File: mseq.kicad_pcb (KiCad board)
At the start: 2 copper layers, 100 x 65 mm, 66 parts, among them J1 Screen_I2C, J2 TC2030-NL, P1 USB_C_Plug_USB2.0, SW1 RESET, SW2 ON/OFF, SW3 MS/SLAVE, SW4 BOOT, U1 SN74AHCT125DR, U2 H11L1M, U3 MCP1703Ax-330xxTT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

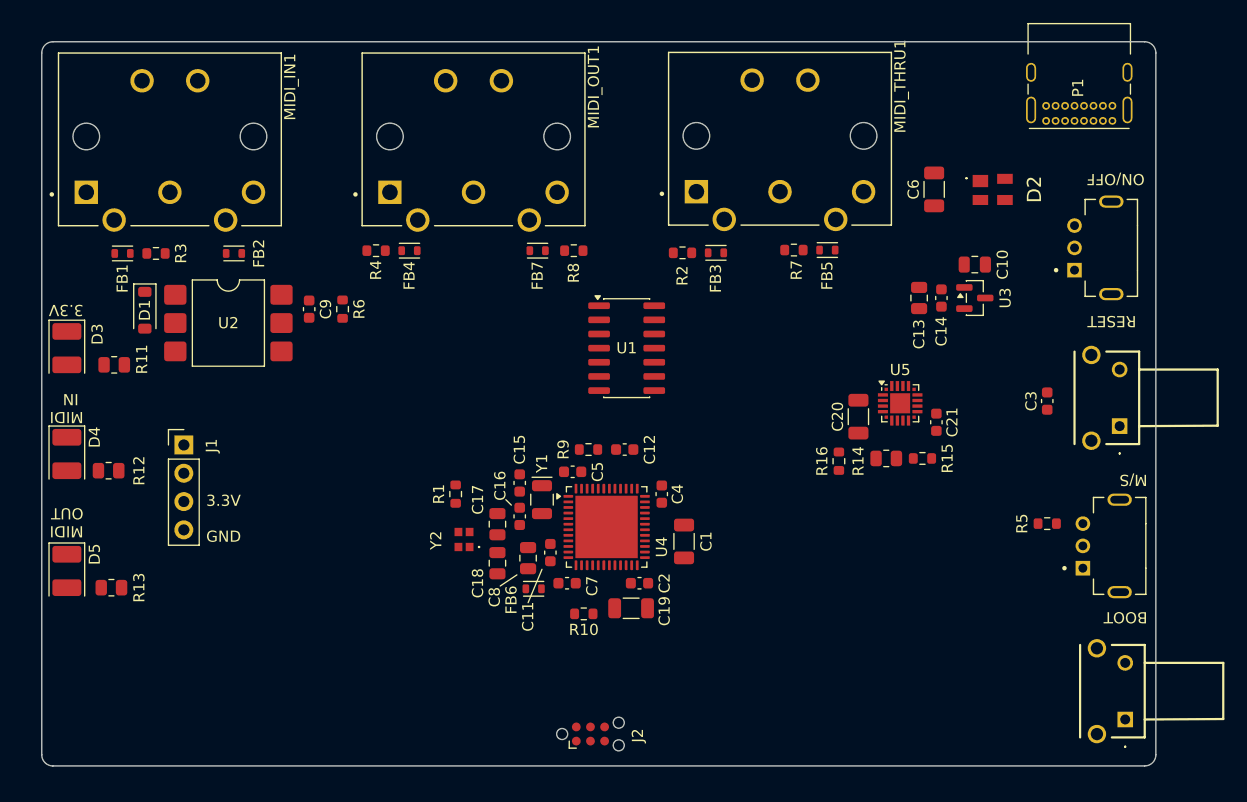
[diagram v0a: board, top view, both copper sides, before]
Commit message: 90% Routing
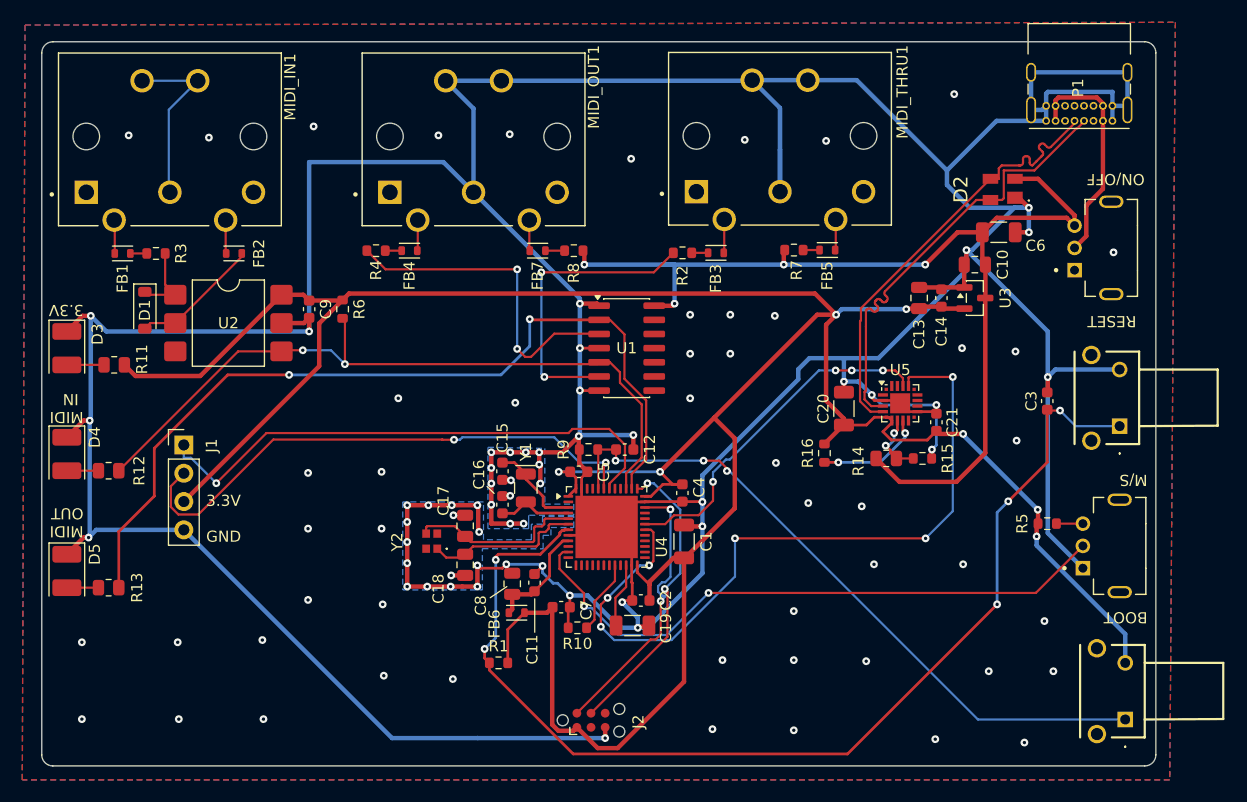
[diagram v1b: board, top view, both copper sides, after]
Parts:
- moved R1 15.6 mm to (91.0, 105.8), turned to 180 degrees
- moved C6 6.96 mm to (135.9, 67.1), turned to 0 degrees
- moved C11 3.05 mm to (94.2, 98.5)
- moved C17 2.90 mm to (88.0, 93.5)
- moved C18 2.90 mm to (88.0, 97.0)
- moved Y2 2.90 mm to (85.0, 94.8)
- moved C8 2.71 mm to (92.2, 98.7)
- moved FB6 2.64 mm to (92.6, 101.2)
- moved C7 2.21 mm to (96.6, 100.8)
- moved C15 1.87 mm to (91.3, 88.5)
- moved C16 1.87 mm to (91.3, 91.5)
- moved C4 1.85 mm to (107.5, 90.5)
- moved Y1 1.79 mm to (93.5, 90.0)
- moved C19 1.56 mm to (103.0, 102.4)
- moved C2 1.56 mm to (103.8, 100.2)
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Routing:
- net GND: track 0.00 -> 543.8 mm, vias 0 -> 104
- net +3.3V: track 0.00 -> 268.8 mm, vias 0 -> 7
- net /NRST: track 0.00 -> 99.4 mm, vias 0 -> 5
- net VBUS: track 0.00 -> 94.5 mm, vias 0 -> 4
- net /A15: track 0.00 -> 78.0 mm, vias 0 -> 2
- net /A9: track 0.00 -> 67.4 mm, vias 0 -> 6
- net /B3: track 0.00 -> 66.5 mm, vias 0 -> 2
- net /BOOT0: track 0.00 -> 61.7 mm, vias 0 -> 3
- net /A1: track 0.00 -> 55.6 mm, vias 0 -> 2
- net /B7: track 0.00 -> 49.1 mm, vias 0 -> 2
- net /B6: track 0.00 -> 48.8 mm, vias 0 -> 1
- net /D-: track 0.00 -> 40.0 mm
- net /D+: track 0.00 -> 40.0 mm
- net /A10: track 0.00 -> 31.4 mm, vias 0 -> 4
- net Net-(R4-Pad2): track 0.00 -> 29.9 mm, vias 0 -> 2
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- added copper zone on B.Cu, net GND
- added copper zone on F.Cu, net GND

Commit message: finish routing
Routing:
- net GND: vias 104 -> 108

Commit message: Last DRC Check
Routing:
- net GND: vias 108 -> 114
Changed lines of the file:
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@@
 	)
 	(segment
+		(start 91.4 97.2)
+		(end 91.7 96.9)
+		(width 0.4)
+		(layer "F.Cu")
+		(net 1)
+	)
+	(segment
 		(start 104.162 91.275)
 		(end 104.138 91.3)
@@
 	)
 	(segment
-		(start 89.35 97.25)
-		(end 89.1 97)
-		(width 0.25)
-		(layer "F.Cu")
-		(net 1)
-	)
-	(segment
 		(start 102.95 96.9875)
 		(end 102.95 98.525)
@@
 	)
 	(segment
-		(start 91.7 96.9)
-		(end 91.35 97.25)
-		(width 0.25)
-		(layer "F.Cu")
-		(net 1)
-	)
-	(segment
 		(start 91.35 90.775)
 		(end 92.025 90.775)
@@
 	)
 	(segment
-		(start 91.35 97.25)
-		(end 89.35 97.25)
-		(width 0.25)
+		(start 89.3 97.2)
+		(end 91.4 97.2)
+		(width 0.4)
 		(layer "F.Cu")
 		(net 1)
@@
 	)
 	(segment
+		(start 89.1 97)
+		(end 89.3 97.2)
+		(width 0.4)
+		(layer "F.Cu")
+		(net 1)
+	)
+	(segment
 		(start 84.6 98.9)
 		(end 86.7 98.9)
@@
 	)
 	(via
+		(at 69.1 81.5)
+		(size 0.7)
+		(drill 0.3)
+		(layers "F.Cu" "B.Cu")
+		(free yes)
+		(net 1)
+	)
+	(via
 		(at 111.8 74.5)
 		(size 0.7)
@@
 	)
 	(via
+		(at 66.5 84.2)
+		(size 0.7)
+		(drill 0.3)
+		(layers "F.Cu" "B.Cu")
+		(free yes)
+		(net 1)
+	)
+	(via
 		(at 82.8 96.8)
 		(size 0.7)
@@
 	)
 	(via
+		(at 82.1 75.9)
+		(size 0.7)
+		(drill 0.3)
+		(layers "F.Cu" "B.Cu")
+		(free yes)
+		(net 1)
+	)
+	(via
 		(at 140.3 80.1)
 		(size 0.7)
@@
 	)
 	(via
+		(at 88.3 75.9)
+		(size 0.7)
+		(drill 0.3)
+		(layers "F.Cu" "B.Cu")
+		(free yes)
+		(net 1)
+	)
+	(via
 		(at 92.05 90.75)
 		(size 0.7)
@@
 	)
 	(via
+		(at 93.9 107.4)
+		(size 0.7)
+		(drill 0.3)
+		(layers "F.Cu" "B.Cu")
+		(free yes)
+		(net 1)
+	)
+	(via
 		(at 84.6 98.9)
 		(size 0.7)
@@
 	)
 	(via
+		(at 142.8 61)
+		(size 0.7)
+		(drill 0.3)
+		(layers "F.Cu" "B.Cu")
+		(free yes)
+		(net 1)
+	)
+	(via
 		(at 108.2 74.5)
 		(size 0.7)
@@
 		(filled_areas_thickness no)
 		(keepout
-			(tracks not_allowed)
+			(tracks allowed)
 			(vias not_allowed)
 			(pads not_allowed)
@@
 		(polygon
 			(pts
-				(xy 89.6 99.4) (xy 89.6 97.6) (xy 89.8 97.6) (xy 89.8 99.6) (xy 82.1 99.6) (xy 82.1 99.4)
+				(xy 89.6 99.4) (xy 89.6 97.1) (xy 89.8 97.1) (xy 89.8 99.6) (xy 82.1 99.6) (xy 82.1 99.4)
 			)
 		)
@@
 		(filled_areas_thickness no)
 		(keepout
-			(tracks not_allowed)
+			(tracks allowed)
 			(vias not_allowed)
 			(pads allowed)
@@
 		(polygon
 			(pts
-				(xy 98 91.6) (xy 95.35 91.6) (xy 95.2 91.5) (xy 95.2 87.1) (xy 95.45 87.1) (xy 95.45 91.35) (xy 95.6 91.45)
+				(xy 98 91.6) (xy 95.35 91.6) (xy 95.2 91.5) (xy 95.2 86.8) (xy 95.45 86.8) (xy 95.45 91.35) (xy 95.6 91.45)
 				(xy 98 91.45)
 			)
@@
 		(filled_areas_thickness no)
 		(keepout
-			(tracks not_allowed)
+			(tracks allowed)
 			(vias not_allowed)
 			(pads not_allowed)
@@
 		(polygon
 			(pts
-				(xy 89.6 97) (xy 89.6 95.5) (xy 94.5 95.5) (xy 94.8 95.1) (xy 94.8 94.2) (xy 95.2 94.2) (xy 95.7 93.7)
+				(xy 89.6 97.2) (xy 89.6 95.5) (xy 94.5 95.5) (xy 94.8 95.1) (xy 94.8 94.2) (xy 95.2 94.2) (xy 95.7 93.7)
 				(xy 95.7 93.55) (xy 96.6 93.55) (xy 96.6 93.7) (xy 96 93.7) (xy 95.2 94.4) (xy 95 94.4) (xy 95 95.1)
-				(xy 94.6 95.7) (xy 89.8 95.7) (xy 89.8 97)
+				(xy 94.6 95.7) (xy 89.8 95.7) (xy 89.8 97.2)
 			)
 		)
@@
 		(filled_areas_thickness no)
 		(keepout
-			(tracks not_allowed)
+			(tracks allowed)
 			(vias not_allowed)
 			(pads not_allowed)
@@
 		(polygon
 			(pts
-				(xy 95.45 86.5) (xy 95.2 86.5) (xy 95.2 86.4) (xy 89.95 86.4) (xy 89.95 93.8) (xy 93.65 93.8) (xy 93.65 93.9)
+				(xy 95.45 86.9) (xy 95.2 86.9) (xy 95.2 86.4) (xy 89.95 86.4) (xy 89.95 93.8) (xy 93.65 93.8) (xy 93.65 93.9)
 				(xy 89.85 93.9) (xy 89.85 86.3) (xy 95.45 86.3)
 			)

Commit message: v0.1.0 done
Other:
- board text added: "MSeq v0.1.0"

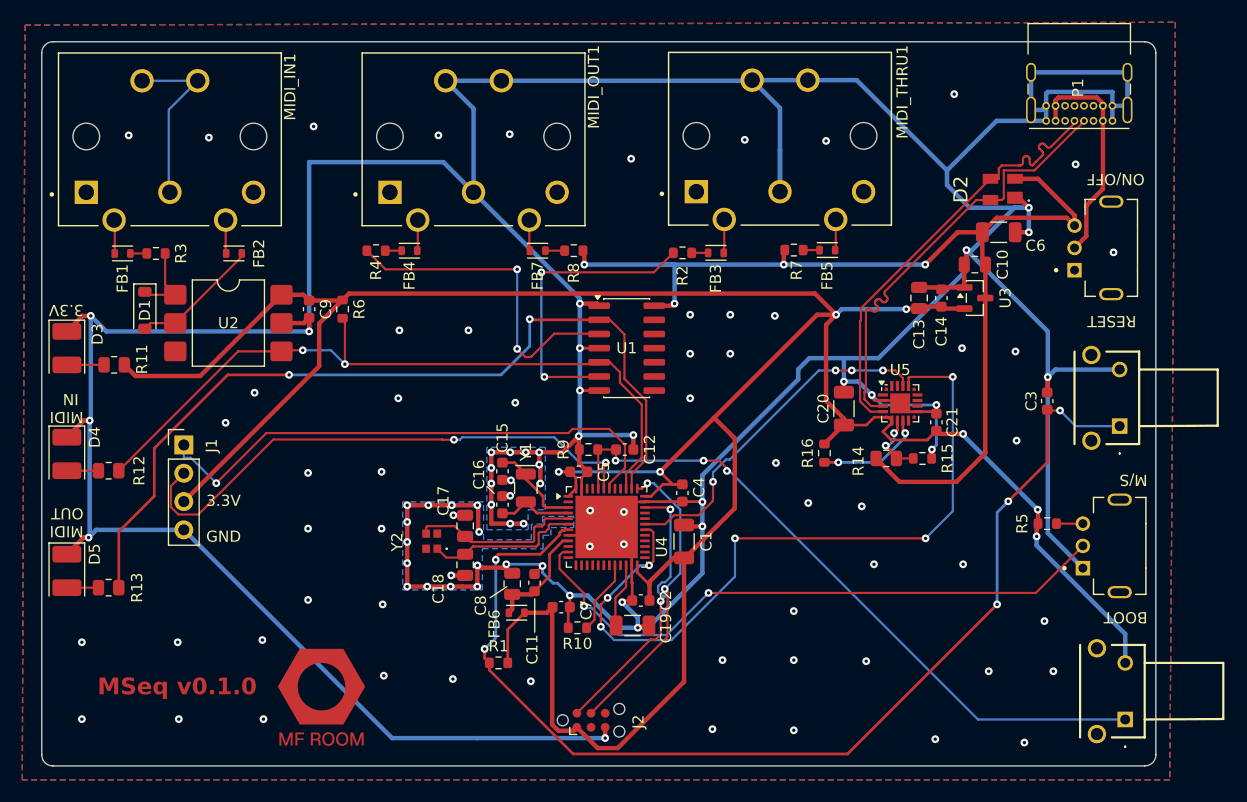
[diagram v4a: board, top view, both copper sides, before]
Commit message: LCSC Part Change, need MCP/MPN
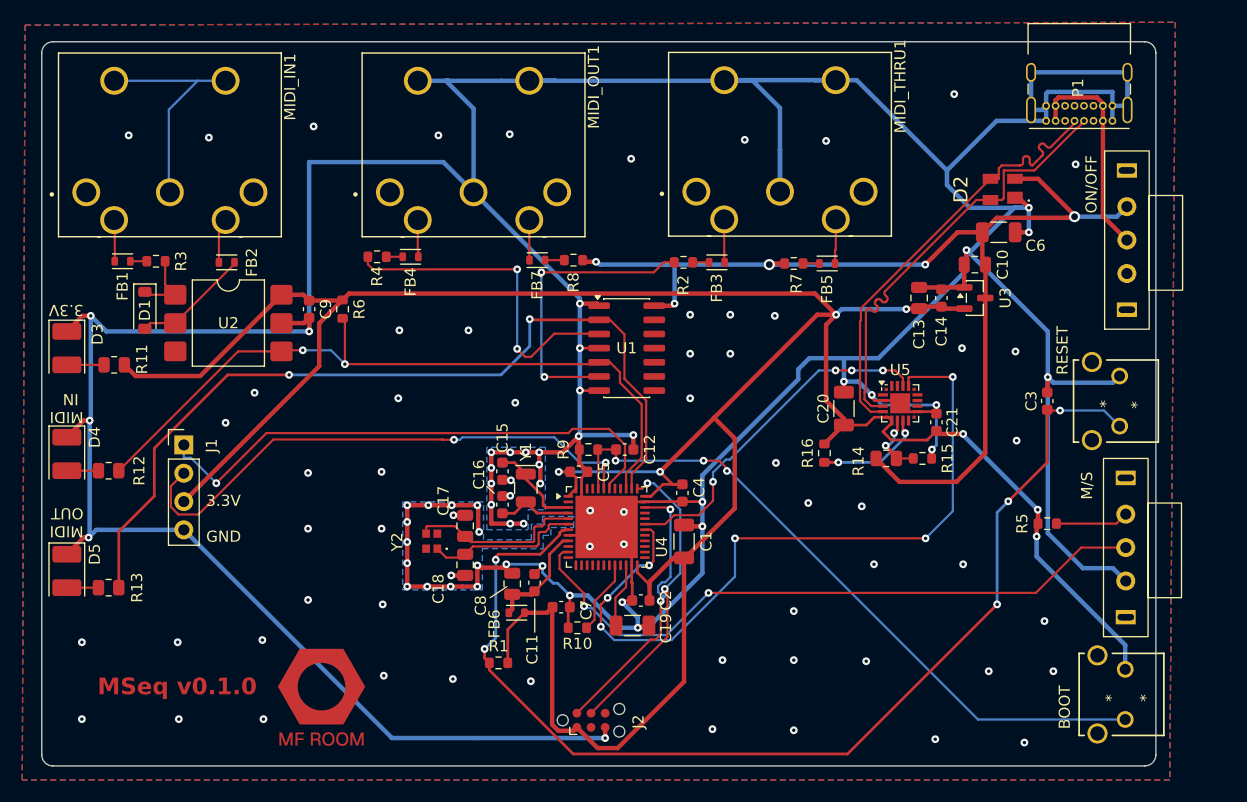
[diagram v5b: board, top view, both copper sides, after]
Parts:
- MIDI_IN1, MIDI_OUT1, MIDI_THRU1: footprint mseq_lib:SWITCHCRAFT_57PC5F -> mseq_lib:DIN-504
- SW1, SW4: footprint mseq_lib:TL6110DF160QP -> mseq_lib:SW2_1825027-A_TEC
- SW2, SW3: footprint mseq_lib:SW_SLW-874744-6A-RA-N-D -> mseq_lib:SK-12E12-G5
- moved SW3 3.20 mm to (147.3, 98.4)
- moved SW2 2.69 mm to (147.4, 70.8)
- moved FB5 1.21 mm to (120.5, 69.9)
- moved R7 1.21 mm to (117.5, 69.9)
- moved FB2 1.03 mm to (66.6, 69.8)
- moved FB3 0.86 mm to (110.6, 69.8)
- moved R2 0.86 mm to (107.6, 69.8)
- moved FB7 0.85 mm to (94.5, 69.6)
- moved R8 0.85 mm to (97.7, 69.6)
- moved FB1 0.70 mm to (57.2, 69.7)
- moved R3 0.70 mm to (60.2, 69.7)
- moved FB4 0.56 mm to (83.1, 69.3)
- moved R4 0.56 mm to (80.1, 69.3)
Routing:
- net GND: track 543.8 -> 557.7 mm, vias 114 -> 113
- net unconnected-(MIDI_IN1-GND-PadG1): track 16.1 -> 21.1 mm
- net Net-(SW3-A): track 2.38 -> 6.58 mm
- net /A1: track 55.6 -> 59.3 mm
- net VBUS: track 94.5 -> 97.9 mm, vias 4 -> 5
- net Net-(FB5-Pad2): track 3.35 -> 4.56 mm
- net Net-(D1-A): track 11.7 -> 10.6 mm
- net Net-(FB2-Pad2): track 3.02 -> 4.05 mm
- net Net-(SW2-B): track 20.4 -> 19.6 mm
- net Net-(FB7-Pad2): track 2.77 -> 3.61 mm
- net Net-(FB3-Pad1): track 3.05 -> 3.87 mm
- net Net-(FB1-Pad2): track 3.02 -> 3.72 mm
- net Net-(D1-K): track 6.93 -> 6.23 mm
- net +3.3V: track 268.8 -> 269.4 mm
- net Net-(FB4-Pad1): track 2.77 -> 3.32 mm

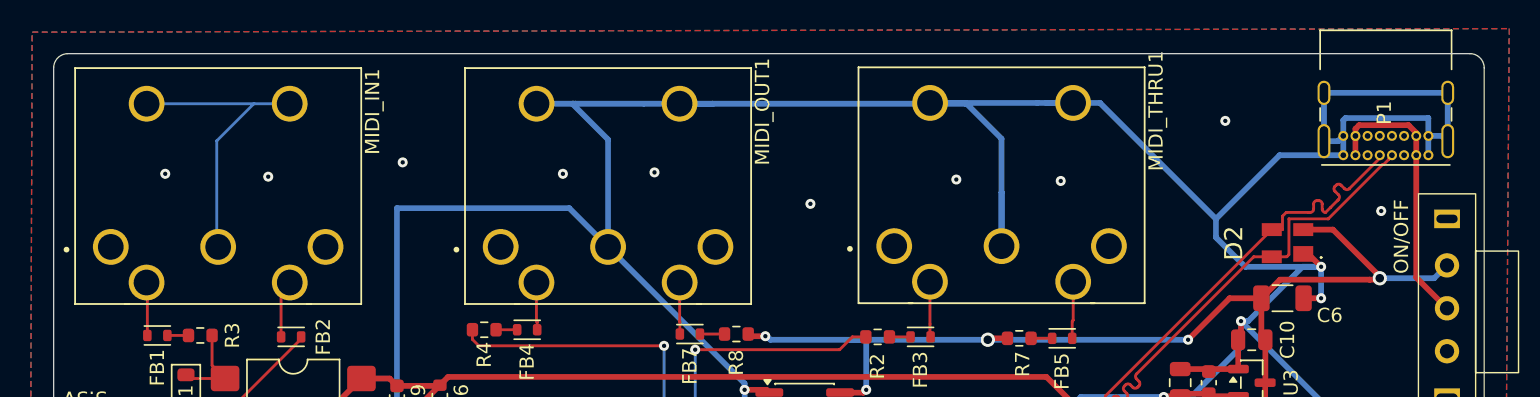
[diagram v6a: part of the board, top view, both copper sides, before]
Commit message: USB connector changed
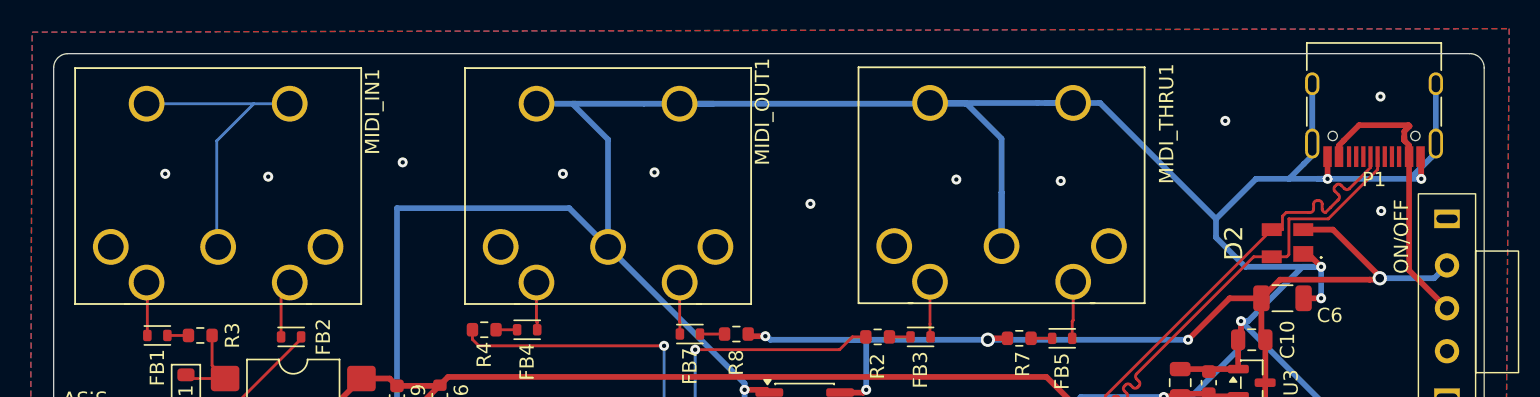
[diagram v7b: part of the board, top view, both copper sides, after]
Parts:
- P1: footprint Connector_USB:USB_C_Receptacle_GCT_USB4085 -> Connector_USB:USB_C_Receptacle_HRO_TYPE-C-31-M-12
- moved P1 5.48 mm to (142.3, 53.2)
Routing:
- net GND: track 557.7 -> 553.4 mm, vias 113 -> 116
- net Net-(SW2-B): track 19.6 -> 20.7 mm
- net /D+: track 40.0 -> 39.5 mm

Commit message: WIP, need to make the board bigger
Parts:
- D3, D4, D5: footprint LED_SMD:LED_PLCC-2_3.4x3.0mm_KA -> LED_SMD:LED_0603_1608Metric
- SW2, SW3: footprint mseq_lib:SK-12E12-G5 -> Button_Switch_THT:SW_Slide_SPDT_Angled_CK_OS102011MA1Q
- Y2: value 25MHz 9pF -> 25MHz 18pF; footprint mseq_lib:XRCGB25M000F1SBJR0 -> Crystal:Crystal_SMD_5032-2Pin_5.0x3.2mm
- moved SW3 1.12 mm to (147.1, 97.3)
- moved SW4 0.57 mm to (146.8, 111.1)
- moved Y2 0.40 mm to (84.8, 95.2)
- moved SW2 0.25 mm to (147.2, 70.8)
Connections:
- Y2 pad 2: (no net) -> /PH0
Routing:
- net Net-(SW2-B): track 20.7 -> 23.4 mm
- net GND: track 553.4 -> 554.9 mm
- net /PH1: track 14.1 -> 14.7 mm
- net Net-(SW3-A): track 6.58 -> 6.05 mm
